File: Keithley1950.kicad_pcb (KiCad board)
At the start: 2 copper layers, 60 x 80 mm, 94 parts, among them J1 Conn_01x14, J2 Conn_01x03, J3 Conn_01x02, K1 Relay_SP2P, K2 Relay_SP2P, K3 Relay_SP3P, K4 Relay_SP2P, K5 Relay_SP2P, K6 Relay_SP3P, K7 Relay_SP3P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

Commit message: Fixes, tweaks, tag rev A
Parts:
- moved H2 1.12 mm to (35.0, 58.0)
- moved C7 0.75 mm to (73.0, 79.8)
- moved C12 0.50 mm to (79.0, 77.8)
- moved C13 0.50 mm to (79.0, 81.2)
- moved C21 0.50 mm to (55.0, 79.0)
- moved C23 0.50 mm to (49.0, 79.0)
- moved C24 0.50 mm to (64.0, 79.0)
- moved C6 0.50 mm to (67.0, 82.0)
- moved C8 0.50 mm to (67.0, 78.5)
- moved C9 0.50 mm to (71.5, 73.8)
- moved K6 0.50 mm to (60.5, 91.0)
- moved K7 0.50 mm to (33.0, 91.0)
- moved R19 0.50 mm to (75.0, 73.8)
- moved R25 0.50 mm to (59.5, 79.0)
- moved TP2 0.50 mm to (72.5, 74.0)
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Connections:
- U2 pad 12: GNDA -> -15V
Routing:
- net GNDA: track 254.4 -> 239.0 mm, vias 19 -> 20
- net -15V: track 119.0 -> 122.8 mm
- net +15V: track 106.4 -> 104.2 mm
- net Net-(C21-Pad2): track 58.4 -> 56.5 mm
- net /1K_EN: track 25.6 -> 24.1 mm
- net Net-(TP4-Pad1): track 4.50 -> 3.22 mm
- net /INPUT_LO: track 84.2 -> 85.4 mm
- net /TRMS_DC_SIGNAL: track 16.1 -> 16.8 mm
- net Net-(K7-Pad5): track 26.7 -> 26.2 mm
- net Net-(C10-Pad1): track 5.47 -> 4.97 mm
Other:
- outline, holes or cut-outs redrawn

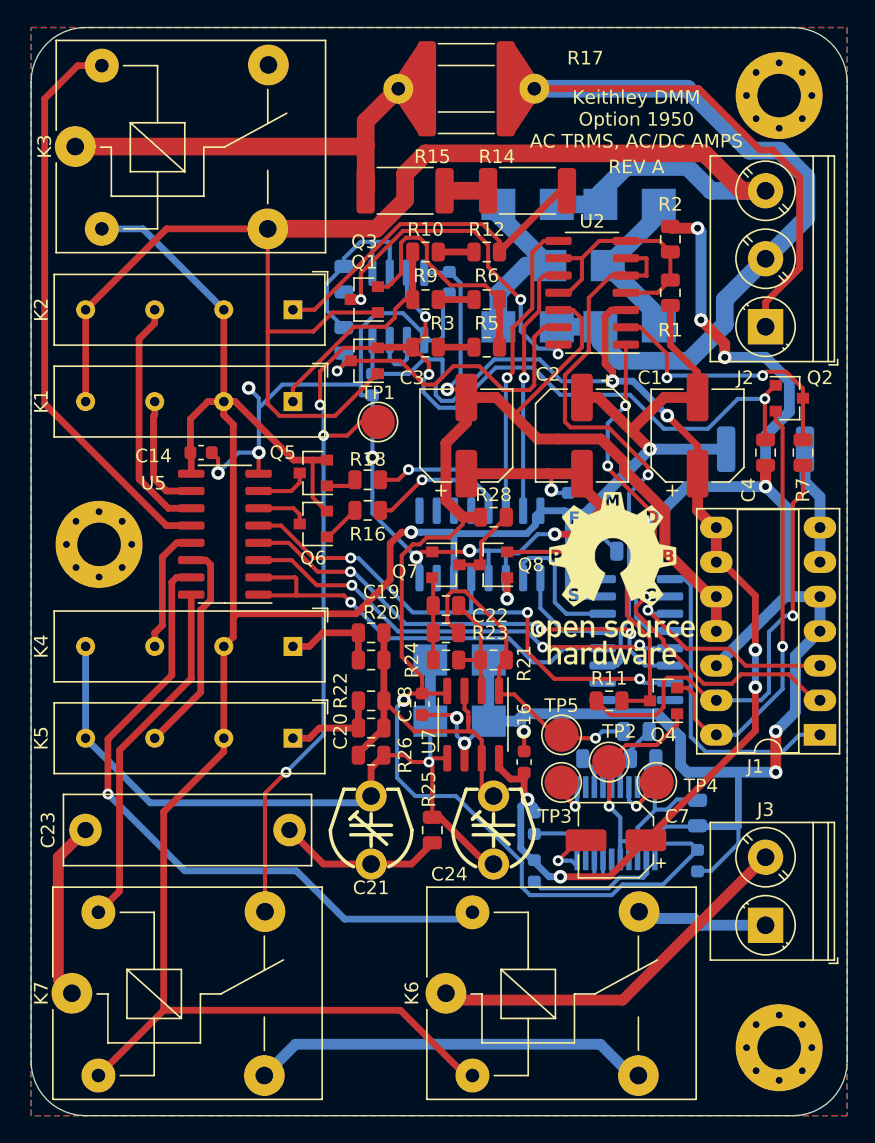
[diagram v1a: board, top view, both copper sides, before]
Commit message: Revision B
1. Clearance for high voltage lines
2. 14 pin connector courtyard overlap
3. 24K resistor is DNP
4. Fix swapped inputs of U7B
5. Change c7 to tantalum type Bx
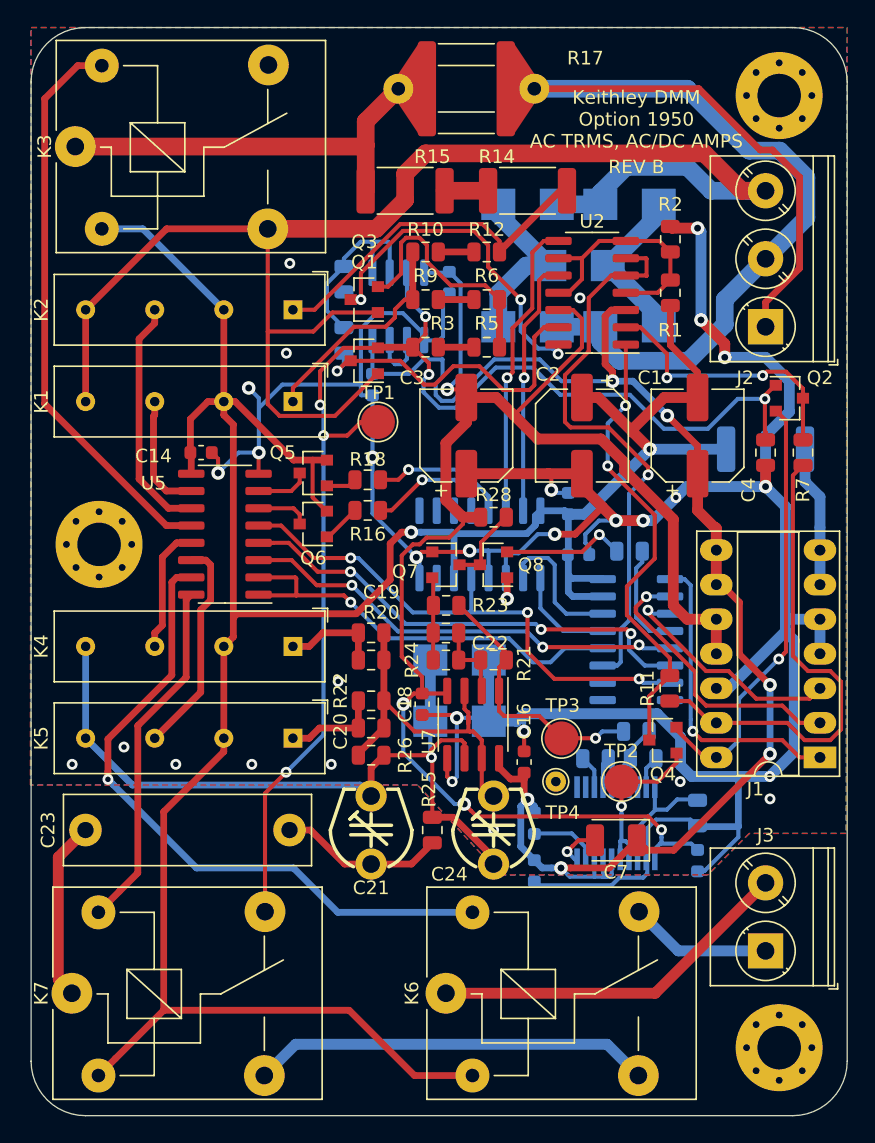
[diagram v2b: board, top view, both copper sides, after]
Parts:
- removed the LOGO*** at (72.8, 60.5)
- removed TP5: TestPoint, TestPoint:TestPoint_Pad_D2.5mm
- C7: footprint Capacitor_SMD:CP_Elec_5x5.4 -> Capacitor_Tantalum_SMD:CP_EIA-3528-21_Kemet-B
- R23: value 24k -> DNP
- TP4: footprint TestPoint:TestPoint_Pad_D2.5mm -> TestPoint:TestPoint_THTPad_D1.5mm_Drill0.7mm
- U1, U7: value TL082 -> TLE2072
- moved LOGO*** 45.0 mm to (42.7, 56.9), turned to 270 degrees
- moved TP4 7.42 mm to (68.6, 75.4), turned to 0 degrees
- moved R11 4.56 mm to (77.0, 68.6), turned to 90 degrees
- moved TP3 3.24 mm to (69.0, 72.3)
- moved Q4 2.89 mm to (76.5, 72.4)
- moved R23 2.02 mm to (60.5, 62.5)
- moved C22 2.02 mm to (60.5, 64.5)
- moved J3 1.88 mm to (84.0, 87.9)
- moved TP2 1.70 mm to (73.4, 75.4)
- moved J1 1.66 mm to (88.0, 73.7)
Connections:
- K3 pad 4: (no net) -> Net-(K3-Pad4)
- TP3 pad 1: Net-(TP3-Pad1) -> Net-(C10-Pad2)
- TP4 pad 1: Net-(TP4-Pad1) -> GNDA
- U3 pad 10: (no net) -> Net-(U3-Pad10)
- U3 pad 11: (no net) -> Net-(U3-Pad11)
- U3 pad 7: (no net) -> Net-(U3-Pad7)
- U3 pad 9: (no net) -> Net-(U3-Pad9)
- U4 pad 1: Net-(TP3-Pad1) -> Net-(U4-Pad1)
- U4 pad 2: (no net) -> Net-(U4-Pad2)
- U4 pad 7: Net-(TP4-Pad1) -> Net-(U4-Pad7)
- U4 pad 8: (no net) -> Net-(U4-Pad8)
- U6 pad 10: (no net) -> Net-(U6-Pad10)
- U6 pad 9: (no net) -> Net-(U6-Pad9)
- U7 pad 5: Net-(C21-Pad2) -> GNDA
- U7 pad 6: GNDA -> Net-(C21-Pad2)
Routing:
- net GNDA: track 239.0 -> 244.6 mm, vias 20 -> 32
- net -15V: track 122.8 -> 117.6 mm, vias 2 -> 4
- net Net-(C10-Pad2): track 24.5 -> 19.6 mm
- net Net-(C21-Pad2): track 56.5 -> 60.0 mm
- net /TRMS_DC_SIGNAL: track 16.8 -> 13.4 mm
- net Net-(TP4-Pad1): track 3.22 -> 0.00 mm, vias 1 -> 0
- net Net-(TP3-Pad1): track 3.13 -> 0.00 mm, vias 1 -> 0
- net Net-(C22-Pad2): track 8.85 -> 6.16 mm
- net +15V: track 104.2 -> 106.8 mm
- net Net-(Q4-Pad3): track 31.8 -> 33.8 mm
- net /SIGNAL_GUARD: track 34.4 -> 36.2 mm, vias 1 -> 0
- net Net-(J1-Pad6): track 8.76 -> 10.3 mm
- net Net-(C7-Pad2): track 4.23 -> 2.70 mm
- net /CLOCK: track 16.1 -> 17.5 mm
- net /RETURN: track 9.51 -> 10.5 mm
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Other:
- board text added: "REV B"
- board text removed: "REV A"
